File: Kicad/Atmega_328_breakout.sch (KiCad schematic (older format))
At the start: 71 parts, among them J1 Jack-DC, J10 Conn_01x06, J11 1x2, J12 1x2, J13 1x2, J14 1x2, J15 1x2, J16 1x2, J17 1x2, J18 1x2, J19 Power_connector, J2 1x2, J20 ADC_Connector, J21 PORB++_connector, J22 PORD_connector, J23 Conn_01x01, J24 Device_Connector, J25 Pin out, J26 Com_header, J27 Power terminal, J28 USB, J3 1x2, J4 1x2, J5 1x2, J6 1x2, J7 1x2, J8 1x2, J9 1x2, Q1 PMOS, SW1 SW_Push, SW2 SW_Push, U1 NCP1117-5, U2 L7805, U3 TL071, U4 ATMEGA328P-AU, U5 MCP1700-33, U6 MCP2221, Y1 Crystal

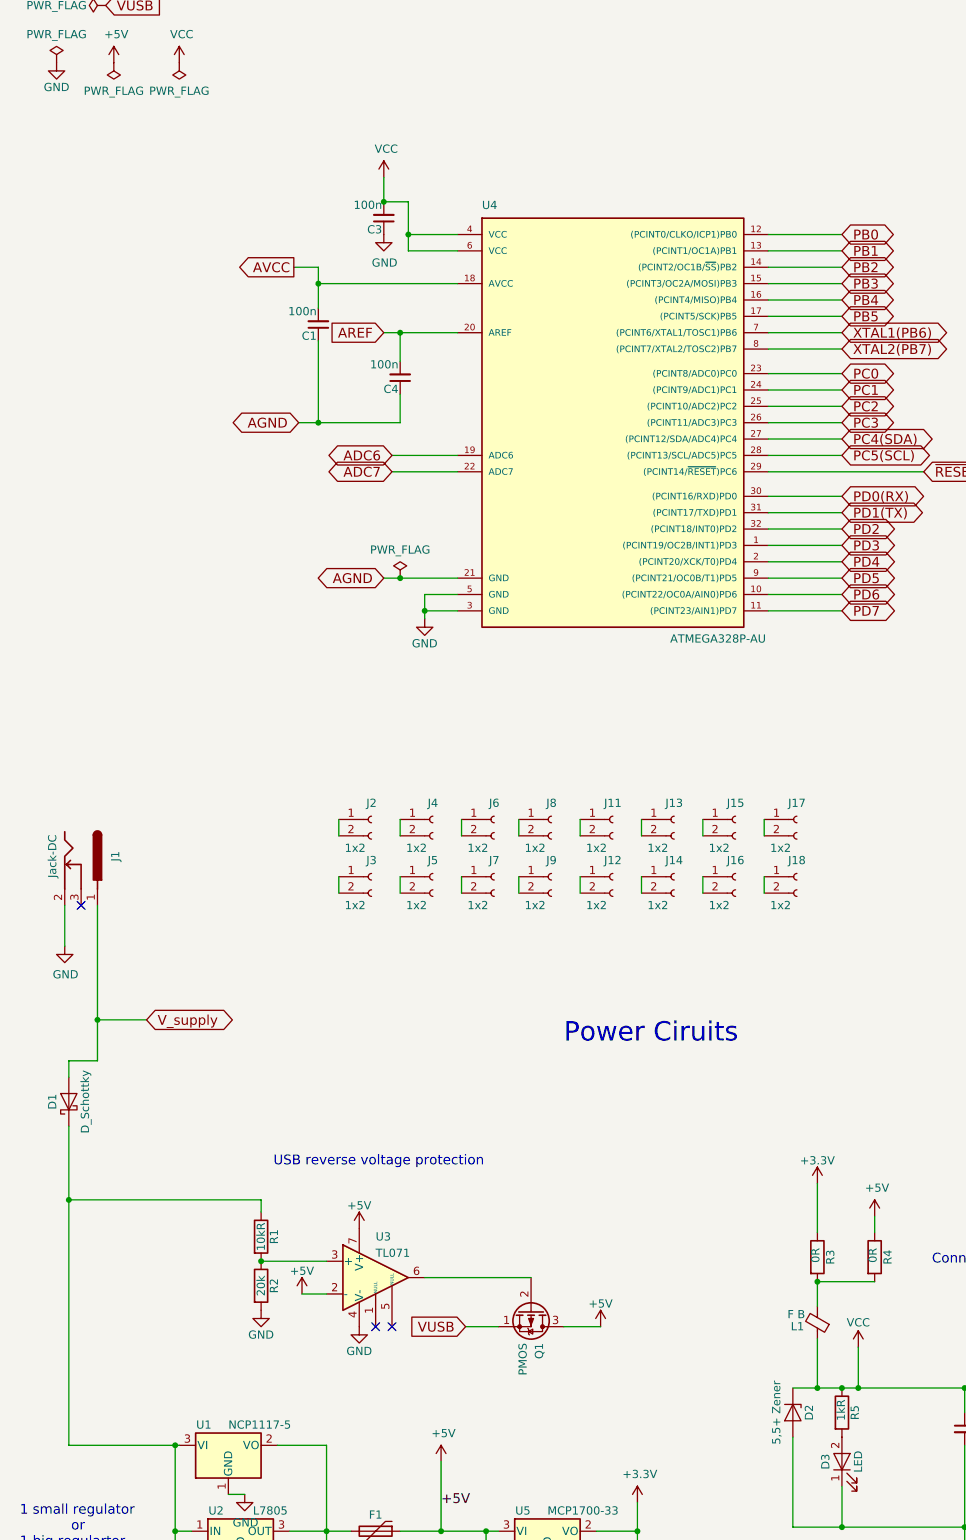
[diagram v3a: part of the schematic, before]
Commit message: added available parts from jlcpcb for bom
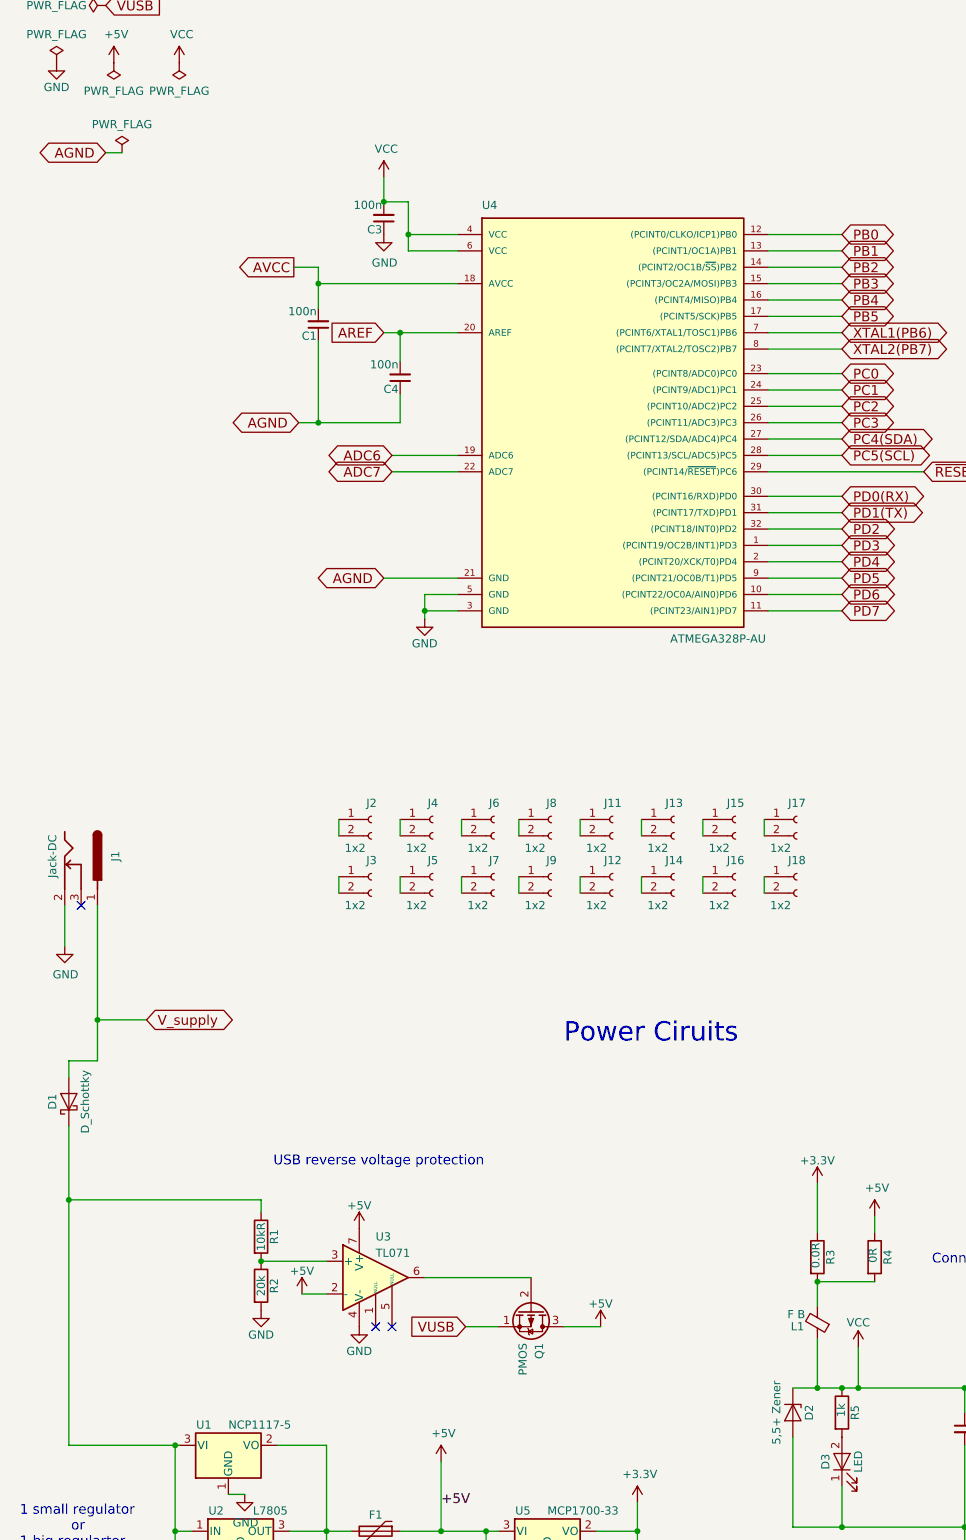
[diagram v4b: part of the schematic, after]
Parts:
- C1, C13, C3, C4, C5, C7, C8, C9: LCSC (none) -> C14663
- C10, C2, C6: LCSC (none) -> C15849
- C11, C12: LCSC (none) -> C1653
- D3, D4: LCSC (none) -> C188728
- R1: footprint Capacitor_SMD:C_0603_1608Metric -> Resistor_SMD:R_0603_1608Metric_Pad0.98x0.95mm_HandSolder; LCSC (none) -> C25804
- R2: footprint Capacitor_SMD:C_0603_1608Metric -> Resistor_SMD:R_0603_1608Metric_Pad0.98x0.95mm_HandSolder; LCSC (none) -> C4184
- R3: value 0R -> 0.0R; footprint Capacitor_SMD:C_0603_1608Metric -> Resistor_SMD:R_0603_1608Metric_Pad0.98x0.95mm_HandSolder
- R4: footprint Capacitor_SMD:C_0603_1608Metric -> Resistor_SMD:R_0603_1608Metric_Pad0.98x0.95mm_HandSolder; LCSC (none) -> C21189
- R5: value 1kR -> 1k; footprint Capacitor_SMD:C_0603_1608Metric -> Resistor_SMD:R_0603_1608Metric_Pad0.98x0.95mm_HandSolder; LCSC (none) -> C21190
- R6: footprint Capacitor_SMD:C_0603_1608Metric -> Resistor_SMD:R_0603_1608Metric_Pad0.98x0.95mm_HandSolder; LCSC (none) -> C23164
- R7: footprint Capacitor_SMD:C_0603_1608Metric -> Resistor_SMD:R_0603_1608Metric_Pad0.98x0.95mm_HandSolder; LCSC (none) -> C23138
- R8: footprint Capacitor_SMD:C_0603_1608Metric -> Resistor_SMD:R_0603_1608Metric_Pad0.98x0.95mm_HandSolder; LCSC (none) -> C21190
- R9: footprint Capacitor_SMD:C_0603_1608Metric -> Resistor_SMD:R_0603_1608Metric_Pad0.98x0.95mm_HandSolder; LCSC (none) -> C25803
- U3: LCSC (none) -> C350565
- U5: LCSC (none) -> C62244
- U6: LCSC (none) -> C130462
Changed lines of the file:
@@
 F 2 "Capacitor_SMD:C_0603_1608Metric_Pad1.08x0.95mm_HandSolder" H 2950 3425 50  0001 C CNN
 F 3 "" H 2950 3425 50  0001 C CNN
+F 4 "C14663" H 2950 3425 50  0001 C CNN "LCSC"
 	1    2950 3425
 	-1   0    0    1
@@
 F 2 "Capacitor_SMD:C_0603_1608Metric_Pad1.08x0.95mm_HandSolder" H 2450 3100 50  0001 C CNN
 F 3 "" H 2450 3100 50  0001 C CNN
+F 4 "C14663" H 2450 3100 50  0001 C CNN "LCSC"
 	1    2450 3100
 	-1   0    0    1
@@
 F 2 "Capacitor_SMD:C_0603_1608Metric_Pad1.08x0.95mm_HandSolder" H 9125 10050 50  0001 C CNN
 F 3 "" H 9125 10050 50  0001 C CNN
+F 4 "C14663" H 9125 10050 50  0001 C CNN "LCSC"
 	1    9125 10050
 	1    0    0    -1
@@
 F 2 "Capacitor_SMD:C_0603_1608Metric_Pad1.08x0.95mm_HandSolder" H 12350 1650 50  0001 C CNN
 F 3 "" H 12350 1650 50  0001 C CNN
+F 4 "C1653" H 12350 1650 50  0001 C CNN "LCSC"
 	1    12350 1650
 	-1   0    0    1
@@
 F 2 "Capacitor_SMD:C_0603_1608Metric_Pad1.08x0.95mm_HandSolder" H 12850 1650 50  0001 C CNN
 F 3 "" H 12850 1650 50  0001 C CNN
+F 4 "C1653" H 12850 1650 50  0001 C CNN "LCSC"
 	1    12850 1650
 	-1   0    0    1
@@
 F 0 "R7" V 9530 9850 50  0000 C CNN
 F 1 "330" V 9450 9850 50  0000 C CNN
-F 2 "Capacitor_SMD:C_0603_1608Metric" V 9380 9850 50  0001 C CNN
+F 2 "Resistor_SMD:R_0603_1608Metric_Pad0.98x0.95mm_HandSolder" V 9380 9850 50  0001 C CNN
 F 3 "" H 9450 9850 50  0001 C CNN
+F 4 "C23138" V 9450 9850 50  0001 C CNN "LCSC"
 	1    9450 9850
 	0    1    1    0
@@
 F 2 "LED_SMD:LED_0805_2012Metric_Pad1.15x1.40mm_HandSolder" H 13900 6350 50  0001 C CNN
 F 3 "" H 13900 6350 50  0001 C CNN
+F 4 "C188728" H 13900 6350 50  0001 C CNN "LCSC"
 	1    13900 6350
 	0    -1   -1   0
@@
 F 0 "R8" V 13980 5950 50  0000 C CNN
 F 1 "1k" V 13901 5951 50  0000 C CNN
-F 2 "Capacitor_SMD:C_0603_1608Metric" V 13830 5950 50  0001 C CNN
+F 2 "Resistor_SMD:R_0603_1608Metric_Pad0.98x0.95mm_HandSolder" V 13830 5950 50  0001 C CNN
 F 3 "" H 13900 5950 50  0001 C CNN
+F 4 "C21190" V 13900 5950 50  0001 C CNN "LCSC"
 	1    13900 5950
 	1    0    0    -1
@@
 P 5500 8800
 F 0 "R3" V 5580 8800 50  0000 C CNN
-F 1 "0R" V 5489 8811 50  0000 C CNN
-F 2 "Capacitor_SMD:C_0603_1608Metric" V 5430 8800 50  0001 C CNN
+F 1 "0.0R" V 5489 8811 50  0000 C CNN
+F 2 "Resistor_SMD:R_0603_1608Metric_Pad0.98x0.95mm_HandSolder" V 5430 8800 50  0001 C CNN
 F 3 "" H 5500 8800 50  0001 C CNN
 	1    5500 8800
@@
 F 0 "R4" V 5930 8800 50  0000 C CNN
 F 1 "0R" V 5839 8811 50  0000 C CNN
-F 2 "Capacitor_SMD:C_0603_1608Metric" V 5780 8800 50  0001 C CNN
+F 2 "Resistor_SMD:R_0603_1608Metric_Pad0.98x0.95mm_HandSolder" V 5780 8800 50  0001 C CNN
 F 3 "" H 5850 8800 50  0001 C CNN
+F 4 "C21189" V 5850 8800 50  0001 C CNN "LCSC"
 	1    5850 8800
 	1    0    0    -1
@@
 F 0 "R6" V 9205 9475 50  0000 C CNN
 F 1 "4,7k" V 9125 9475 50  0000 C CNN
-F 2 "Capacitor_SMD:C_0603_1608Metric" V 9055 9475 50  0001 C CNN
+F 2 "Resistor_SMD:R_0603_1608Metric_Pad0.98x0.95mm_HandSolder" V 9055 9475 50  0001 C CNN
 F 3 "" H 9125 9475 50  0001 C CNN
+F 4 "C23164" V 9125 9475 50  0001 C CNN "LCSC"
 	1    9125 9475
 	1    0    0    -1
@@
 Text Notes 6200 8850 0    60   ~ 0
 Connect the selected VCC, not both
-$Comp
-L Atmega_328_breakout-rescue:C_Small C3
-U 1 1 5A76BD1D
-P 2850 2450
-F 0 "C3" H 2860 2520 50  0000 L CNN
-F 1 "100n" H 2860 2370 50  0000 L CNN
-F 2 "Capacitor_SMD:C_0603_1608Metric_Pad1.08x0.95mm_HandSolder" H 2850 2450 50  0001 C CNN
-F 3 "" H 2850 2450 50  0001 C CNN
-	1    2850 2450
-	-1   0    0    1
-$EndComp
 NoConn ~ 15300 9100
 NoConn ~ 13600 9200
@@
 Wire Wire Line
 	2950 3325 2950 3150
-Wire Wire Line
-	2850 4650 2950 4650
 Wire Wire Line
 	3100 4750 3100 4850
@@
 F 2 "Package_TO_SOT_SMD:SOT-23" H 1900 10150 50  0001 C CNN
 F 3 "" H 2000 9700 50  0001 C CNN
+F 4 "" H 1900 9950 50  0001 C CNN "LCSC"
 	1    1900 9950
 	1    0    0    -1
@@
 F 0 "R1" V 2180 8675 50  0000 C CNN
 F 1 "10kR" V 2100 8675 50  0000 C CNN
-F 2 "Capacitor_SMD:C_0603_1608Metric" V 2030 8675 50  0001 C CNN
+F 2 "Resistor_SMD:R_0603_1608Metric_Pad0.98x0.95mm_HandSolder" V 2030 8675 50  0001 C CNN
 F 3 "" H 2100 8675 50  0001 C CNN
+F 4 "C25804" V 2100 8675 50  0001 C CNN "LCSC"
 	1    2100 8675
 	1    0    0    -1
@@
 F 0 "R2" V 2180 8975 50  0000 C CNN
 F 1 "20k" V 2100 8975 50  0000 C CNN
-F 2 "Capacitor_SMD:C_0603_1608Metric" V 2030 8975 50  0001 C CNN
+F 2 "Resistor_SMD:R_0603_1608Metric_Pad0.98x0.95mm_HandSolder" V 2030 8975 50  0001 C CNN
 F 3 "" H 2100 8975 50  0001 C CNN
+F 4 "C4184" V 2100 8975 50  0001 C CNN "LCSC"
 	1    2100 8975
 	1    0    0    -1
@@
 F 2 "Package_SO:SOIC-8_3.9x4.9mm_P1.27mm" H 2850 8975 50  0001 C CNN
 F 3 "" H 2950 9075 50  0001 C CNN
+F 4 "C350565" H 2800 8925 50  0001 C CNN "LCSC"
 	1    2800 8925
 	1    0    0    -1
@@
 F 2 "Capacitor_SMD:C_0603_1608Metric_Pad1.08x0.95mm_HandSolder" H 4400 10650 50  0001 C CNN
 F 3 "" H 4400 10650 50  0001 C CNN
+F 4 "C14663" H 4400 10650 50  0001 C CNN "LCSC"
 	1    4400 10650
 	-1   0    0    1
@@
 F 2 "Capacitor_SMD:C_0603_1608Metric_Pad1.08x0.95mm_HandSolder" H 1575 10675 50  0001 C CNN
 F 3 "" H 1575 10675 50  0001 C CNN
+F 4 "C15849" H 1575 10675 50  0001 C CNN "LCSC"
 	1    1575 10675
 	-1   0    0    1
@@
 F 2 "Capacitor_SMD:C_0603_1608Metric_Pad1.08x0.95mm_HandSolder" H 3475 10650 50  0001 C CNN
 F 3 "" H 3475 10650 50  0001 C CNN
+F 4 "C15849" H 3475 10650 50  0001 C CNN "LCSC"
 	1    3475 10650
 	-1   0    0    1
@@
 F 2 "Capacitor_SMD:C_0603_1608Metric_Pad1.08x0.95mm_HandSolder" H 2500 10650 50  0001 C CNN
 F 3 "" H 2500 10650 50  0001 C CNN
+F 4 "C14663" H 2500 10650 50  0001 C CNN "LCSC"
 	1    2500 10650
 	-1   0    0    1
@@
 F 2 "Capacitor_SMD:C_0603_1608Metric_Pad1.08x0.95mm_HandSolder" H 15400 6100 50  0001 C CNN
 F 3 "" H 15400 6100 50  0001 C CNN
+F 4 "C14663" H 15400 6100 50  0001 C CNN "LCSC"
 	1    15400 6100
 	-1   0    0    1
@@
 F 0 "R9" V 15144 5486 50  0000 C CNN
 F 1 "100kR" V 14950 5500 50  0000 C CNN
-F 2 "Capacitor_SMD:C_0603_1608Metric" V 14980 5500 50  0001 C CNN
+F 2 "Resistor_SMD:R_0603_1608Metric_Pad0.98x0.95mm_HandSolder" V 14980 5500 50  0001 C CNN
 F 3 "" H 15050 5500 50  0001 C CNN
+F 4 "C25803" V 15050 5500 50  0001 C CNN "LCSC"
 	1    15050 5500
 	1    0    0    -1
@@
 F 2 "Capacitor_SMD:C_0603_1608Metric_Pad1.08x0.95mm_HandSolder" H 11300 3850 50  0001 C CNN
 F 3 "" H 11300 3850 50  0001 C CNN
+F 4 "C15849" H 11300 3850 50  0001 C CNN "LCSC"
 	1    11300 3850
 	-1   0    0    1
@@
 F 2 "Capacitor_SMD:C_0603_1608Metric_Pad1.08x0.95mm_HandSolder" H 6400 9850 50  0001 C CNN
 F 3 "" H 6400 9850 50  0001 C CNN
+F 4 "C14663" H 6400 9850 50  0001 C CNN "LCSC"
 	1    6400 9850
 	1    0    0    -1
@@
 F 2 "LED_SMD:LED_0805_2012Metric_Pad1.15x1.40mm_HandSolder" H 5650 10050 50  0001 C CNN
 F 3 "" H 5650 10050 50  0001 C CNN
+F 4 "C188728" H 5650 10050 50  0001 C CNN "LCSC"
 	1    5650 10050
 	0    -1   -1   0
@@
 P 5650 9750
 F 0 "R5" V 5730 9750 50  0000 C CNN
-F 1 "1kR" V 5645 9765 50  0000 C CNN
-F 2 "Capacitor_SMD:C_0603_1608Metric" V 5580 9750 50  0001 C CNN
+F 1 "1k" V 5645 9765 50  0000 C CNN
+F 2 "Resistor_SMD:R_0603_1608Metric_Pad0.98x0.95mm_HandSolder" V 5580 9750 50  0001 C CNN
 F 3 "" H 5650 9750 50  0001 C CNN
+F 4 "C21190" V 5650 9750 50  0001 C CNN "LCSC"
 	1    5650 9750
 	1    0    0    -1
@@
 	2850 2350 2850 2200
 Wire Wire Line
-	2850 2350 3000 2350
-Connection ~ 2850 2350
-Wire Wire Line
 	3000 2350 3000 2550
 $Comp
@@
 F 2 "Package_TO_SOT_SMD:SOT-23" H 3850 10700 50  0001 C CNN
 F 3 "" H 3850 10475 50  0001 C CNN
+F 4 "C62244" H 3850 10475 50  0001 C CNN "LCSC"
 	1    3850 10475
 	1    0    0    -1
@@
 	1    0    0    -1
 $EndComp
-$Comp
-L power:PWR_FLAG #FLG02
-U 1 1 605FC6F2
-P 2950 4650
-F 0 "#FLG02" H 2950 4725 50  0001 C CNN
-F 1 "PWR_FLAG" H 2950 4823 50  0000 C CNN
-F 2 "" H 2950 4650 50  0001 C CNN
-F 3 "~" H 2950 4650 50  0001 C CNN
-	1    2950 4650
-	1    0    0    -1
-$EndComp
-Connection ~ 2950 4650
-Wire Wire Line
-	2950 4650 3300 4650
 Wire Wire Line
 	7850 2200 7000 2200
@@
 F 2 "Package_SO:TSSOP-14_4.4x5mm_P0.65mm" H 12950 8700 60  0001 C CNN
 F 3 "" H 12950 8700 60  0001 C CNN
+F 4 "C130462" H 13025 8700 50  0001 C CNN "LCSC"
 	1    13025 8700
 	1    0    0    -1
@@
 	1    0    0    -1
 $EndComp
+Wire Wire Line
+	1150 2050 1250 2050
+Text GLabel 1150 2050 0    60   BiDi ~ 0
+AGND
+$Comp
+L power:PWR_FLAG #FLG0104
+U 1 1 5F90D195
+P 1250 2050
+F 0 "#FLG0104" H 1250 2125 50  0001 C CNN
+F 1 "PWR_FLAG" H 1250 2223 50  0000 C CNN
+F 2 "" H 1250 2050 50  0001 C CNN
+F 3 "~" H 1250 2050 50  0001 C CNN
+	1    1250 2050
+	1    0    0    -1
+$EndComp
+Wire Wire Line
+	2850 4650 3300 4650
+Connection ~ 2850 2350
+Wire Wire Line
+	2850 2350 3000 2350
+$Comp
+L Atmega_328_breakout-rescue:C_Small C3
+U 1 1 5A76BD1D
+P 2850 2450
+F 0 "C3" H 2860 2520 50  0000 L CNN
+F 1 "100n" H 2860 2370 50  0000 L CNN
+F 2 "Capacitor_SMD:C_0603_1608Metric_Pad1.08x0.95mm_HandSolder" H 2850 2450 50  0001 C CNN
+F 3 "" H 2850 2450 50  0001 C CNN
+F 4 "C14663" H 2850 2450 50  0001 C CNN "LCSC"
+	1    2850 2450
+	-1   0    0    1
+$EndComp
 $EndSCHEMATC
